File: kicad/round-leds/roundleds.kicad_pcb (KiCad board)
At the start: 2 copper layers, 21.8 x 21.8 mm, 9 parts, among them P1 CONN_01X02

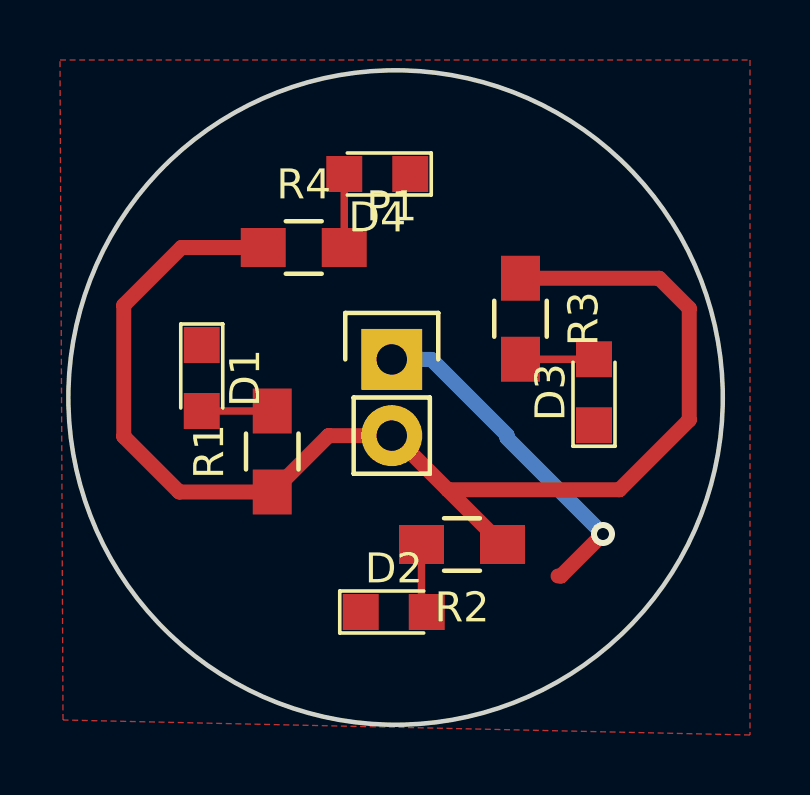
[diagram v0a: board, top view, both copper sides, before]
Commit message: round leds: Add one more GND plane
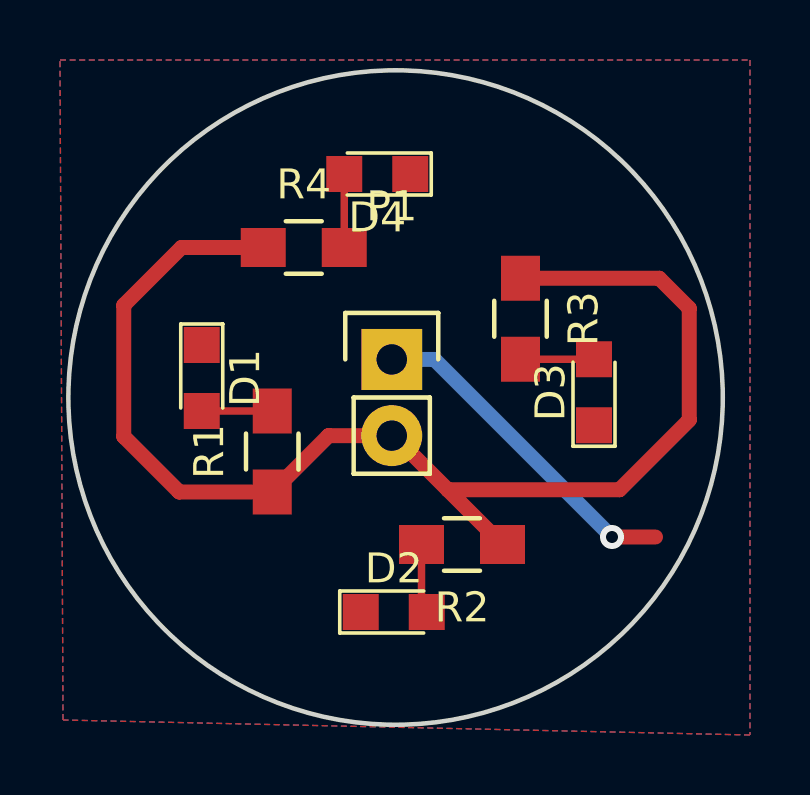
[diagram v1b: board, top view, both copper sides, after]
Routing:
- added copper zone on B.Cu, net GND
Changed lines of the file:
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@@
     (thickness 1.6)
     (drawings 1)
-    (tracks 27)
+    (tracks 24)
     (zones 0)
     (modules 9)
@@
   (gr_circle (center 40.386 27.051) (end 35.306 17.399) (layer Edge.Cuts) (width 0.15))
   (segment (start 33.925 27.5) (end 36.275 27.5) (width 0.25) (layer F.Cu) (net 1))
-  (segment (start 40.259 25.781) (end 41.581 25.781) (width 0.5) (layer B.Cu) (net 2))
-  (segment (start 45.9 33) (end 45.8 33) (width 0.5) (layer F.Cu) (net 2))
-  (segment (start 47.3 31.6) (end 45.9 33) (width 0.5) (layer F.Cu) (net 2))
-  (via (at 47.3 31.6) (size 0.8) (drill 0.4) (layers F.Cu B.Cu) (net 2))
-  (segment (start 44.1 28.4) (end 47.3 31.6) (width 0.5) (layer B.Cu) (net 2))
-  (segment (start 44.1 28.3) (end 44.1 28.4) (width 0.5) (layer B.Cu) (net 2))
-  (segment (start 41.581 25.781) (end 44.1 28.3) (width 0.5) (layer B.Cu) (net 2))
+  (segment (start 40.259 25.781) (end 41.681 25.781) (width 0.5) (layer B.Cu) (net 2))
+  (segment (start 47.6 31.7) (end 49.05 31.7) (width 0.5) (layer F.Cu) (net 2))
+  (via (at 47.6 31.7) (size 0.8) (drill 0.4) (layers F.Cu B.Cu) (net 2))
+  (segment (start 41.681 25.781) (end 47.6 31.7) (width 0.5) (layer B.Cu) (net 2))
   (segment (start 41.25 31.95) (end 41.25 34.025) (width 0.25) (layer F.Cu) (net 3))
   (segment (start 41.25 34.025) (end 41.425 34.2) (width 0.25) (layer F.Cu) (net 3))
@@
       )
     )
+  )
+  (zone (net 2) (net_name GND) (layer B.Cu) (hatch edge 0.508)
+    (connect_pads (clearance 0.508))
+    (min_thickness 0.254)
+    (fill yes (arc_segments 16) (thermal_gap 0.508) (thermal_bridge_width 0.508))
+    (polygon
+      (pts
+        (xy 52.2 38.3) (xy 29.3 37.8) (xy 29.2 15.8) (xy 52.2 15.8)
+      )
+    )
